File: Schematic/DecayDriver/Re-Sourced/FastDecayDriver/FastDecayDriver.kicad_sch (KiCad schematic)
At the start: 11 parts

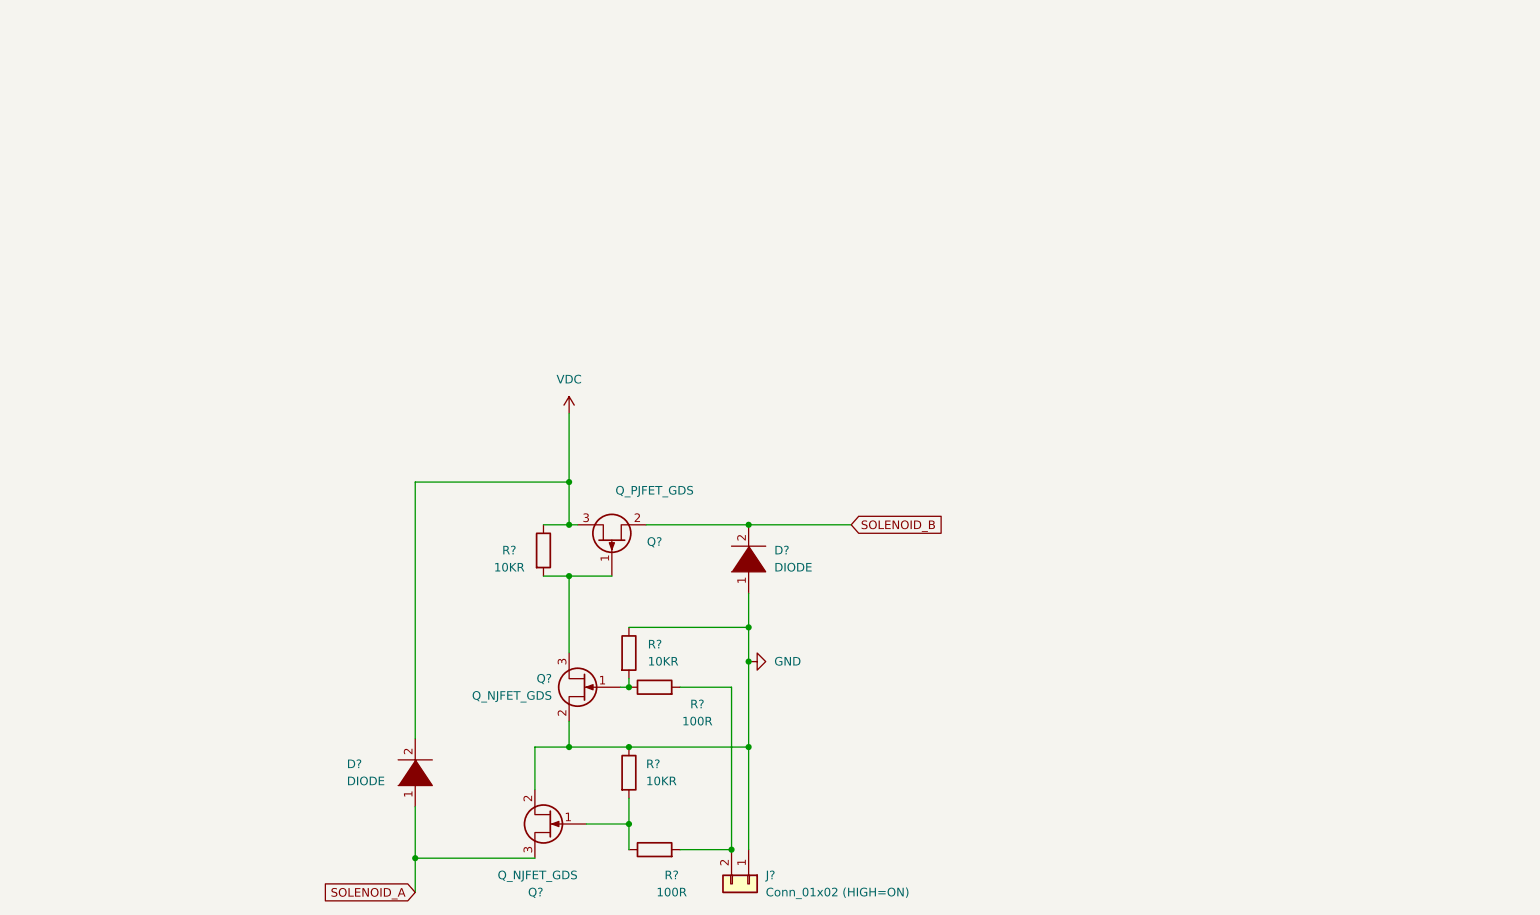
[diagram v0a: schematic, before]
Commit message: begin work on new PCB
2 layers with fast decay driver
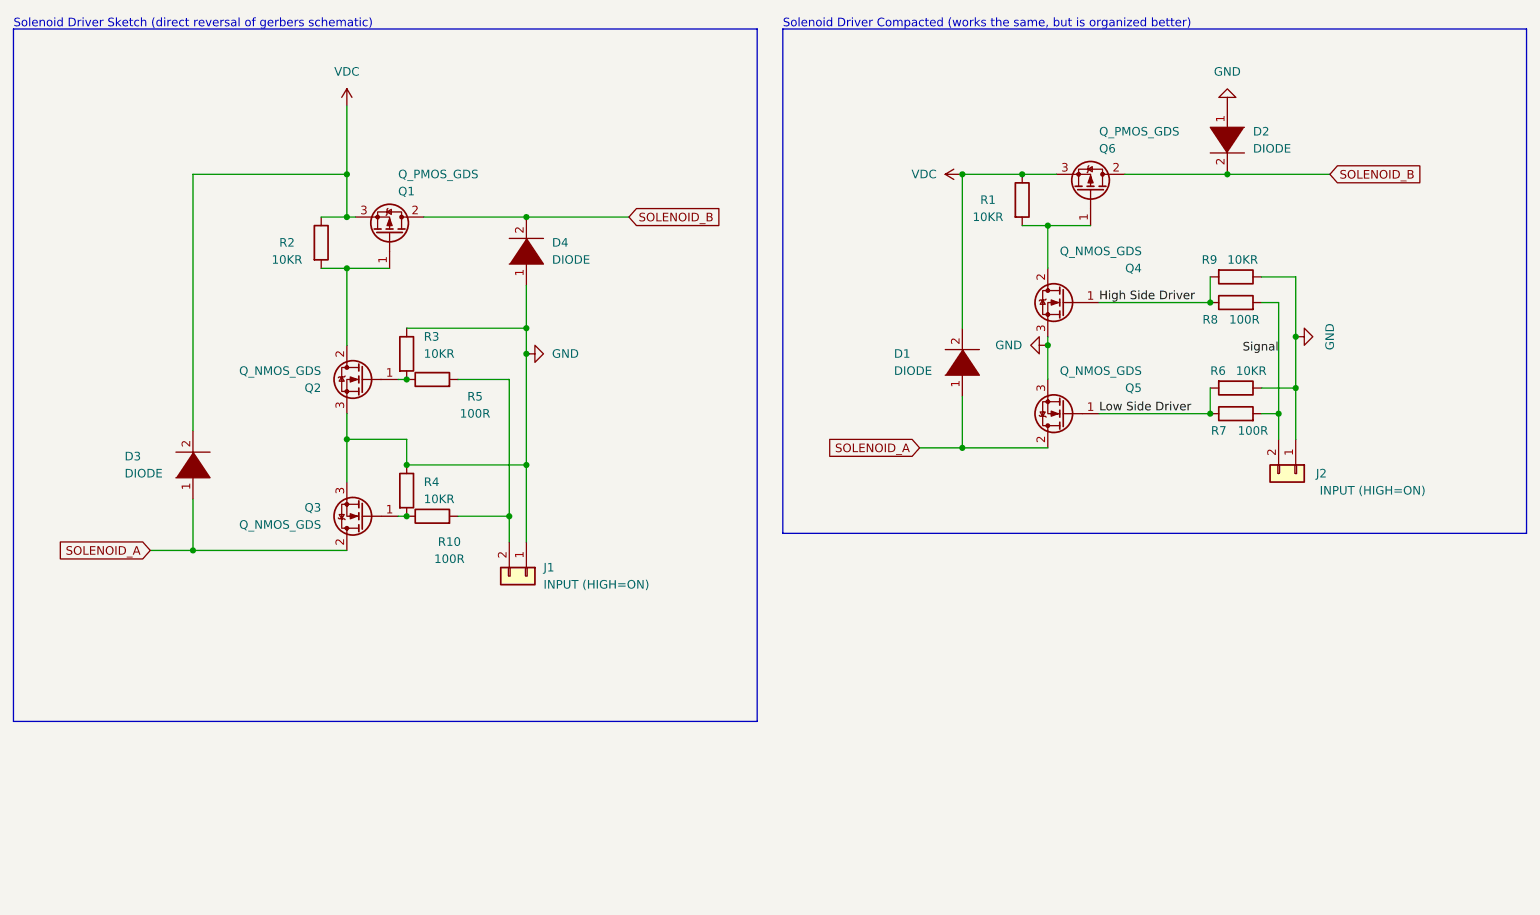
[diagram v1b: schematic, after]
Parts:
- removed Q? (x2): Q_NJFET_GDS, symbol Device:Q_NJFET_GDS
- removed Q?: Q_PJFET_GDS, symbol Device:Q_PJFET_GDS
- added D1, D2: DIODE, Diode_THT:D_DO-41_SOD81_P7.62mm_Horizontal, symbol pspice:DIODE
- added J2: INPUT (HIGH=ON), symbol Connector_Generic:Conn_01x02
- added Q1: Q_PMOS_GDS, symbol Device:Q_PMOS_GDS
- added Q2, Q3: Q_NMOS_GDS, symbol Device:Q_NMOS_GDS
- added Q4, Q5: Q_NMOS_GDS, Package_TO_SOT_THT:TO-220-3_Horizontal_TabDown, symbol Device:Q_NMOS_GDS
- added Q6: Q_PMOS_GDS, Package_TO_SOT_THT:TO-220-3_Horizontal_TabDown, symbol Device:Q_PMOS_GDS
- added R1, R6, R9: 10KR, Resistor_THT:R_Axial_DIN0207_L6.3mm_D2.5mm_P7.62mm_Horizontal, symbol Device:R
- added R7, R8: 100R, Resistor_THT:R_Axial_DIN0207_L6.3mm_D2.5mm_P7.62mm_Horizontal, symbol Device:R
- J1: renamed from J?; value Conn_01x02 (HIGH=ON) -> INPUT (HIGH=ON)
- gave numbers to parts that had none: 7
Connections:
- net GND: now also D2.1 (K), J2.1 (Pin_1), Q2.3 (S), Q3.3 (S), Q4.3 (S), Q5.3 (S), R6.1, R9.1
- net SOLENOID_A: now also D1.1 (K), Q3.2 (D), Q5.2 (D)
- net SOLENOID_B: now also D2.2 (A), Q1.2 (D), Q6.2 (D)
- net VDC: now also D1.2 (A), Q1.3 (S), Q6.3 (S), R1.1
- net at R2.2: now also Q1.1 (G), Q2.2 (D)
- net at R10.1, R4.2: now also Q3.1 (G)
- net at R3.2, R5.1: now also Q2.1 (G)
- new net: Q4.2 (D), Q6.1 (G), R1.2
- new net High Side Driver: Q4.1 (G), R8.1, R9.2
- new net Low Side Driver: Q5.1 (G), R6.2, R7.1
- new net Signal: J2.2 (Pin_2), R7.2, R8.2
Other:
- note added: "Solenoid Driver Compacted (works the same, but is organized better)"
- note added: "Solenoid Driver Sketch (direct reversal of gerbers schematic)"
- title: (none) -> Fast Decay Solenoid Driver prototypes
- moved on the sheet: D3, D4, J1, R10, R2, R3, R4, R5
